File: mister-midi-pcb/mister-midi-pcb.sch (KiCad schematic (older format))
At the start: 15 parts, among them J1 Midi In, J2 USB3_A, J3 Midi Out, J4 Midi Thru, U1 H11L1

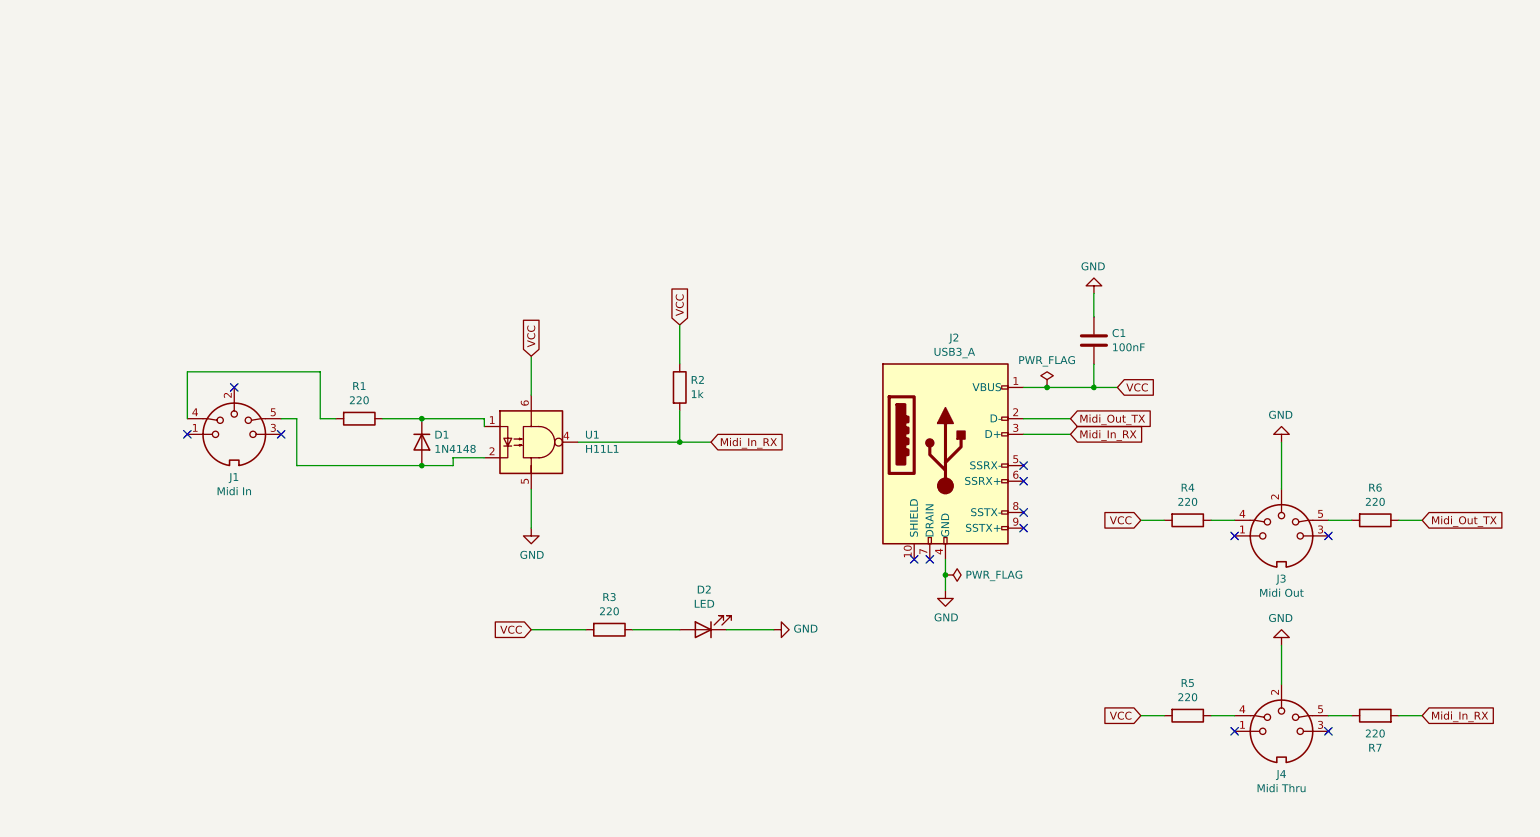
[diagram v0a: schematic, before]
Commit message: reworked pcb with 3.3v
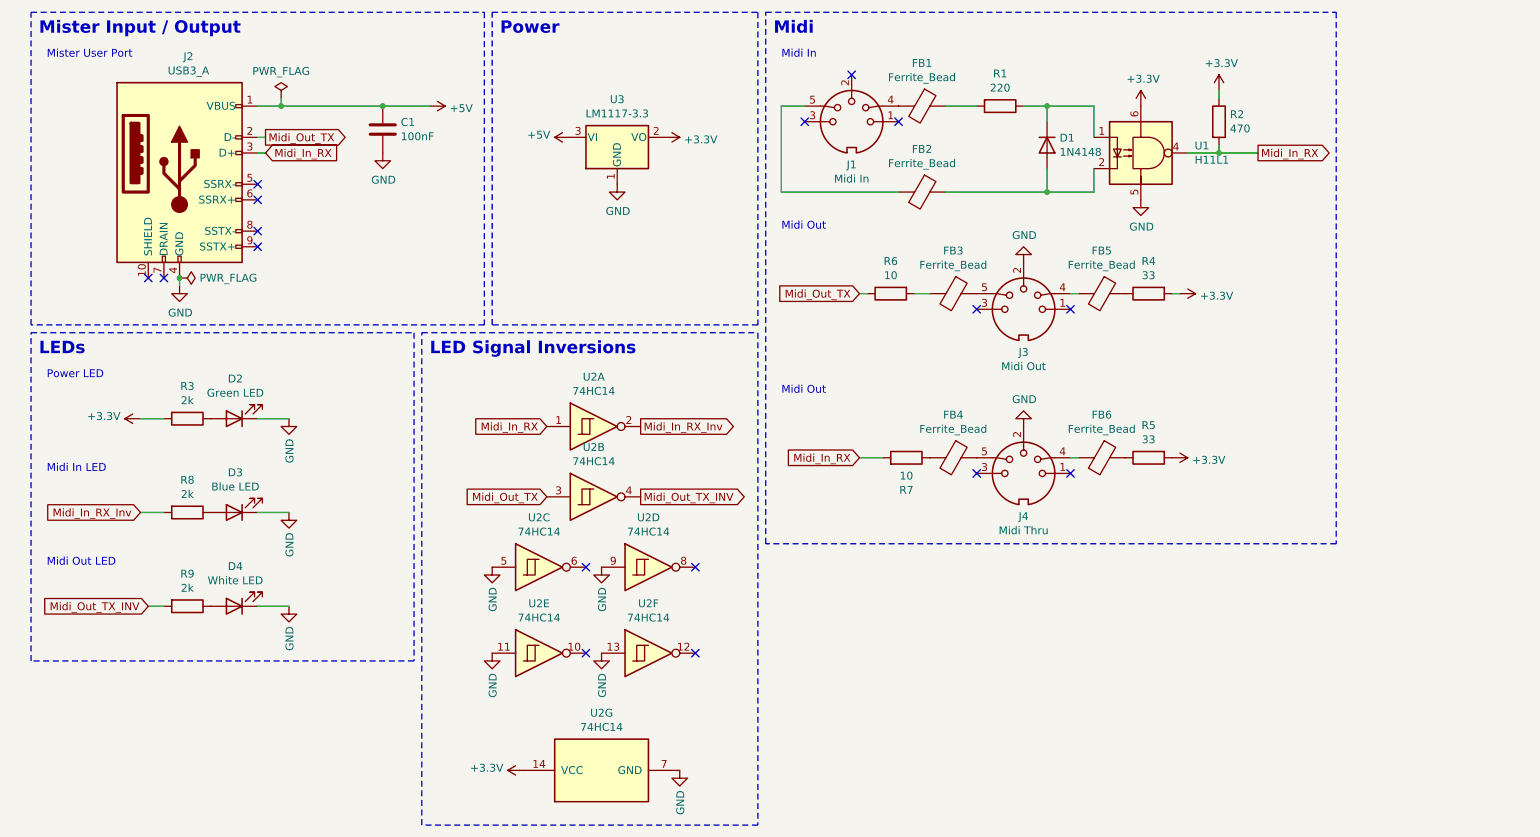
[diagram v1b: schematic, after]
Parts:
- added D3: Blue LED, LED_SMD:LED_0805_2012Metric_Pad1.15x1.40mm_HandSolder, symbol Device:LED
- added D4: White LED, LED_SMD:LED_0805_2012Metric_Pad1.15x1.40mm_HandSolder, symbol Device:LED
- added FB1, FB2, FB3, FB4, FB5, FB6: Ferrite_Bead, Capacitor_SMD:C_0805_2012Metric_Pad1.18x1.45mm_HandSolder, symbol Device:Ferrite_Bead
- added R8, R9: 2k, Resistor_SMD:R_0805_2012Metric_Pad1.20x1.40mm_HandSolder, symbol Device:R
- added U2: 74HC14, Package_SO:SO-14_3.9x8.65mm_P1.27mm, symbol 74xx:74HC14
- added U3: LM1117-3.3, Package_TO_SOT_SMD:SOT-223-3_TabPin2, symbol Regulator_Linear:LM1117-3.3
- D2: value LED -> Green LED
- R2: value 1k -> 470
- R3: value 220 -> 2k
- R4, R5: value 220 -> 33
- R6, R7: value 220 -> 10
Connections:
- net GND: now also C1.2, D3.1 (K), D4.1 (K), U2.11, U2.13, U2.5, U2.7 (GND), U2.9, U3.1 (GND); no longer C1.1
- net Midi_In_RX: now also U2.1
- net Midi_Out_TX: now also U2.3
- net at J1.4: now also FB1.2; no longer R1.2
- net at D1.2 (A), U1.2: now also FB2.1; no longer J1.5
- net at J3.4: now also FB5.2; no longer R4.1
- net at J3.5: now also FB3.1; no longer R6.2
- net at J4.4: now also FB6.2; no longer R5.1
- net at J4.5: now also FB4.1; no longer R7.1
- net VCC renamed +3V3
- net +3V3: now also U2.14 (VCC), U3.2 (VO); no longer C1.2, J2.1 (VBUS)
- new net: FB2.2, J1.5
- new net: FB1.1, R1.2
- new net: FB4.2, R7.1
- new net: FB3.2, R6.2
- new net: FB5.1, R4.1
- new net: FB6.1, R5.1
- new net: D3.2 (A), R8.1
- new net: D4.2 (A), R9.1
- new net +5V: C1.1, J2.1 (VBUS), U3.3 (VI)
- new net Midi_In_RX_Inv: R8.2, U2.2
- new net Midi_Out_TX_INV: R9.2, U2.4
- no-connect marks 13 -> 17
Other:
- note added: "LED Signal Inversions"
- note added: "LEDs"
- note added: "Midi"
- note added: "Midi In"
- note added: "Midi In LED"
- note added: "Midi Out"
- note added: "Midi Out LED"
- note added: "Mister Input / Output\n"
- note added: "Mister User Port"
- note added: "Power LED"
- note added: "Power\n"
- moved on the sheet: C1, D1, D2, J1, J2, J3, J4, R1, R2, R3, R4, R5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

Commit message: out and thru go through buffer now.
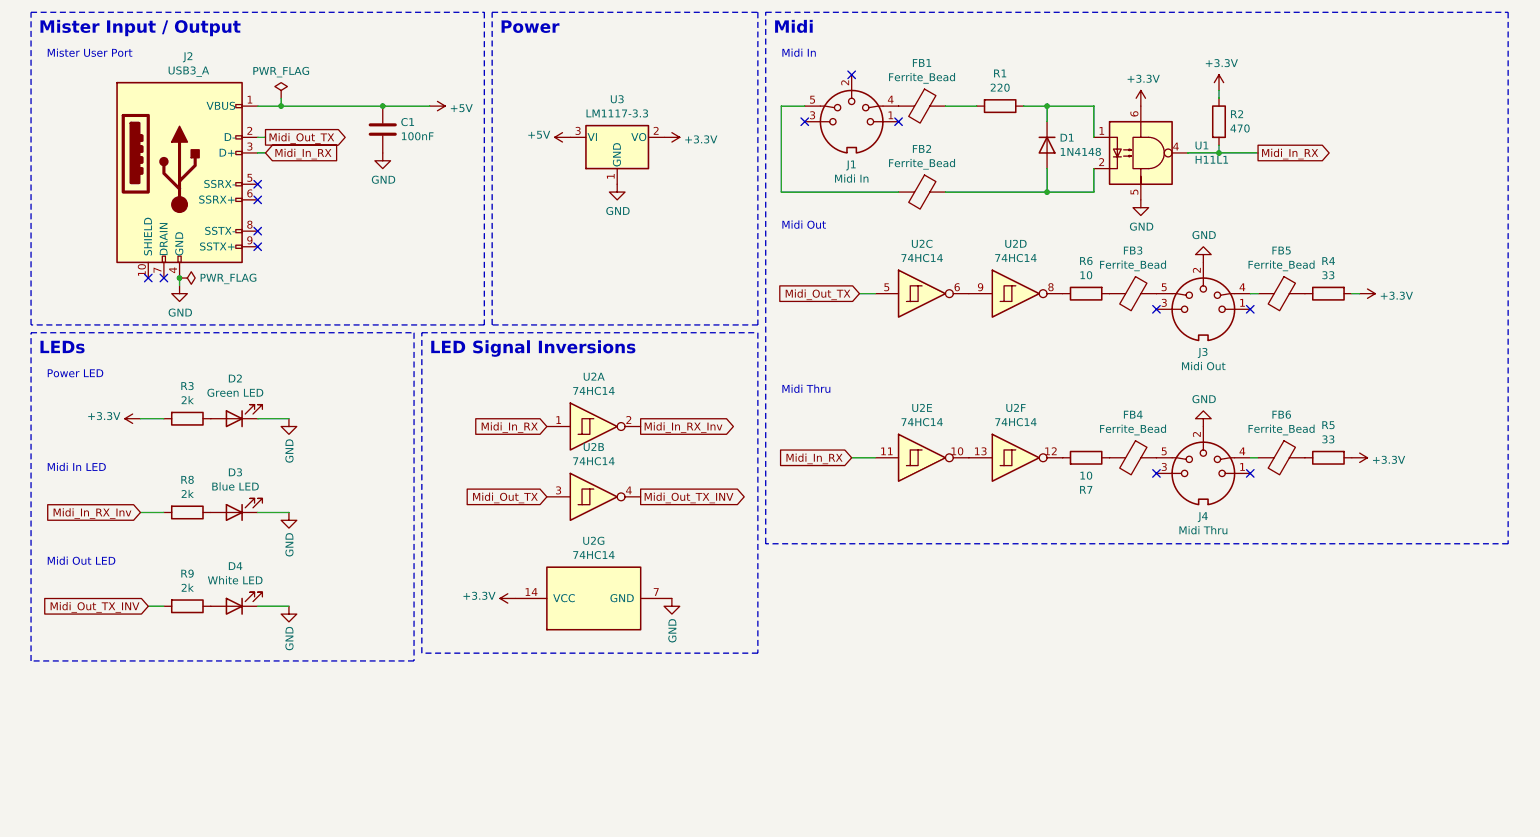
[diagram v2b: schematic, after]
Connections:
- net GND: no longer U2.11, U2.13, U2.5, U2.9
- net Midi_In_RX: now also U2.11; no longer R7.2
- net Midi_Out_TX: now also U2.5; no longer R6.1
- net at U2.6: now also U2.9
- net at U2.8: now also R6.1
- net at U2.10: now also U2.13
- net at U2.12: now also R7.2
- no-connect marks 17 -> 13
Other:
- note added: "Midi Thru"
- moved on the sheet: FB3, FB4, FB5, FB6, J3, J4, R4, R5, R6, R7, U2C, U2D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

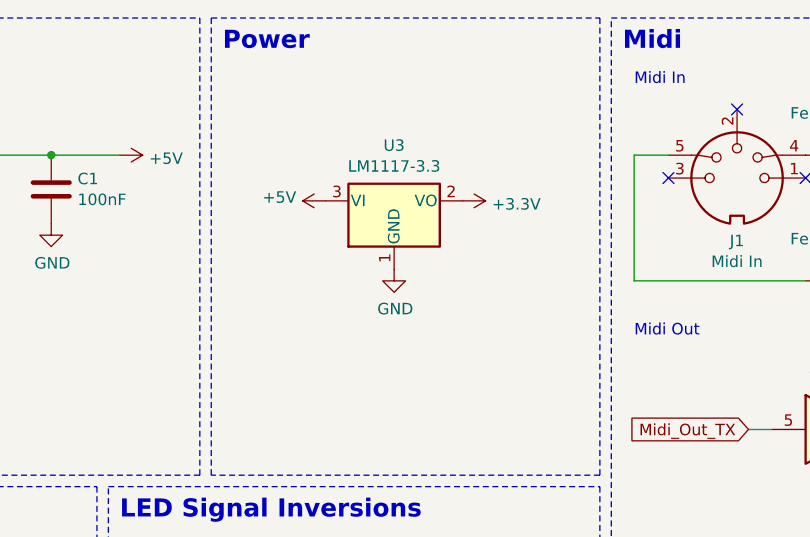
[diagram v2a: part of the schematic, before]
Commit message: added capacitors for ldo
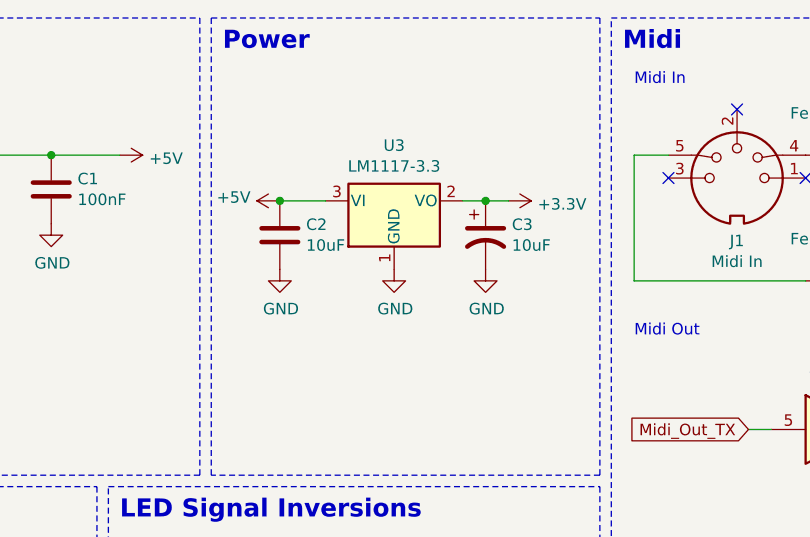
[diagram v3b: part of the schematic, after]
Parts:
- added C2: 10uF, Capacitor_SMD:C_0805_2012Metric_Pad1.18x1.45mm_HandSolder, symbol Device:C
- added C3: 10uF, Capacitor_Tantalum_SMD:CP_EIA-3216-18_Kemet-A_Pad1.58x1.35mm_HandSolder, symbol Device:CP1
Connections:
- net +3V3: now also C3.1
- net +5V: now also C2.1
- net GND: now also C2.2, C3.2
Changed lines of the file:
@@
 L power:+5V #PWR0108
 U 1 1 60D75B57
-P 3950 1350
-F 0 "#PWR0108" H 3950 1200 50  0001 C CNN
-F 1 "+5V" V 3965 1478 50  0000 L CNN
-F 2 "" H 3950 1350 50  0001 C CNN
-F 3 "" H 3950 1350 50  0001 C CNN
-	1    3950 1350
+P 3750 1350
+F 0 "#PWR0108" H 3750 1200 50  0001 C CNN
+F 1 "+5V" V 3765 1478 50  0000 L CNN
+F 2 "" H 3750 1350 50  0001 C CNN
+F 3 "" H 3750 1350 50  0001 C CNN
+	1    3750 1350
 	0    -1   -1   0
 $EndComp
@@
 L power:+3.3V #PWR0109
 U 1 1 60D77140
-P 4550 1350
-F 0 "#PWR0109" H 4550 1200 50  0001 C CNN
-F 1 "+3.3V" V 4565 1478 50  0000 L CNN
-F 2 "" H 4550 1350 50  0001 C CNN
-F 3 "" H 4550 1350 50  0001 C CNN
-	1    4550 1350
+P 4750 1350
+F 0 "#PWR0109" H 4750 1200 50  0001 C CNN
+F 1 "+3.3V" V 4765 1478 50  0000 L CNN
+F 2 "" H 4750 1350 50  0001 C CNN
+F 3 "" H 4750 1350 50  0001 C CNN
+	1    4750 1350
 	0    1    1    0
 $EndComp
@@
 Wire Wire Line
 	5800 2350 5900 2350
+$Comp
+L Device:C C2
+U 1 1 60D782FE
+P 3750 1500
+F 0 "C2" H 3865 1546 50  0000 L CNN
+F 1 "10uF" H 3865 1455 50  0000 L CNN
+F 2 "Capacitor_SMD:C_0805_2012Metric_Pad1.18x1.45mm_HandSolder" H 3788 1350 50  0001 C CNN
+F 3 "~" H 3750 1500 50  0001 C CNN
+	1    3750 1500
+	1    0    0    -1
+$EndComp
+Wire Wire Line
+	3750 1350 3950 1350
+Connection ~ 3750 1350
+$Comp
+L power:GND #PWR0117
+U 1 1 60D7B2EE
+P 3750 1650
+F 0 "#PWR0117" H 3750 1400 50  0001 C CNN
+F 1 "GND" H 3755 1477 50  0000 C CNN
+F 2 "" H 3750 1650 50  0001 C CNN
+F 3 "" H 3750 1650 50  0001 C CNN
+	1    3750 1650
+	1    0    0    -1
+$EndComp
+$Comp
+L Device:CP1 C3
+U 1 1 60D7C1F1
+P 4650 1500
+F 0 "C3" H 4765 1546 50  0000 L CNN
+F 1 "10uF" H 4765 1455 50  0000 L CNN
+F 2 "Capacitor_Tantalum_SMD:CP_EIA-3216-18_Kemet-A_Pad1.58x1.35mm_HandSolder" H 4650 1500 50  0001 C CNN
+F 3 "~" H 4650 1500 50  0001 C CNN
+	1    4650 1500
+	1    0    0    -1
+$EndComp
+Wire Wire Line
+	4550 1350 4650 1350
+Connection ~ 4650 1350
+Wire Wire Line
+	4650 1350 4750 1350
+$Comp
+L power:GND #PWR0118
+U 1 1 60D7F63C
+P 4650 1650
+F 0 "#PWR0118" H 4650 1400 50  0001 C CNN
+F 1 "GND" H 4655 1477 50  0000 C CNN
+F 2 "" H 4650 1650 50  0001 C CNN
+F 3 "" H 4650 1650 50  0001 C CNN
+	1    4650 1650
+	1    0    0    -1
+$EndComp
 $EndSCHEMATC

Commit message: v1.1 of the midi pcb. fixed a couple of problems from the first prototype board.
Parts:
- C2: footprint Capacitor_SMD:C_0805_2012Metric_Pad1.18x1.45mm_HandSolder -> Capacitor_Tantalum_SMD:CP_EIA-3216-18_Kemet-A_Pad1.58x1.35mm_HandSolder
- J2: footprint Connector_USB:USB3_A_Molex_48393-001 -> samacsys:GSB3111113HR
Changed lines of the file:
@@
 F 0 "J2" H 1507 2267 50  0000 C CNN
 F 1 "USB3_A" H 1507 2176 50  0000 C CNN
-F 2 "Connector_USB:USB3_A_Molex_48393-001" H 1600 1650 50  0001 C CNN
+F 2 "samacsys:GSB3111113HR" H 1600 1650 50  0001 C CNN
 F 3 "~" H 1600 1650 50  0001 C CNN
 	1    1450 1550
@@
 F 0 "C2" H 3865 1546 50  0000 L CNN
 F 1 "10uF" H 3865 1455 50  0000 L CNN
-F 2 "Capacitor_SMD:C_0805_2012Metric_Pad1.18x1.45mm_HandSolder" H 3788 1350 50  0001 C CNN
+F 2 "Capacitor_Tantalum_SMD:CP_EIA-3216-18_Kemet-A_Pad1.58x1.35mm_HandSolder" H 3788 1350 50  0001 C CNN
 F 3 "~" H 3750 1500 50  0001 C CNN
 	1    3750 1500
